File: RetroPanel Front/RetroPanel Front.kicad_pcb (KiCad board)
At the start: 2 copper layers, 100 x 22.9 mm, 11 parts, among them J1 Front Panel, M1 Mounting_Pin, M2 Mounting_Pin, M3 Mounting_Pin, M4 Mounting_Pin, SW1 TURBO, SW2 POWER, SW3 RESET, U1 3641AH

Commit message: Layout first draft
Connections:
- J1 pad 10: /7S_D1 -> /7S_F
- J1 pad 11: /7S_D2 -> /7S_E
- J1 pad 12: /7S_D3 -> /7S_D
- J1 pad 13: /7S_D4 -> /7S_DP
- J1 pad 14: SW_PWR1 -> /7S_C
- J1 pad 15: SW_PWR2 -> /7S_G
- J1 pad 16: LED_PWR1 -> /7S_D4
- J1 pad 17: LED_PWR2 -> /7S_D2
- J1 pad 18: SW_TURBO1 -> /7S_D3
- J1 pad 19: SW_TURBO2 -> /7S_B
- J1 pad 2: /7S_A -> SW_PWR1
- J1 pad 20: LED_TURBO1 -> SW_TURBO1
- J1 pad 21: LED_TURBO2 -> SW_TURBO2
- J1 pad 22: SW_RES1 -> LED_TURBO1
- J1 pad 23: SW_RES2 -> LED_TURBO2
- J1 pad 3: /7S_B -> SW_PWR2
- J1 pad 4: /7S_C -> LED_PWR1
- J1 pad 5: /7S_D -> LED_PWR2
- J1 pad 6: /7S_E -> SW_RESET1
- J1 pad 7: /7S_F -> SW_RESET2
- J1 pad 8: /7S_G -> /7S_D1
- J1 pad 9: /7S_DP -> /7S_A
- SW3 pad 2: SW_RES1 -> SW_RESET1
- SW3 pad 3: SW_RES2 -> SW_RESET2
- SW3 pad 5: SW_RES1 -> SW_RESET1
- SW3 pad 6: SW_RES2 -> SW_RESET2
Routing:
- net SW_TURBO1: track 0.00 -> 48.6 mm
- net LED_TURBO1: track 0.00 -> 38.7 mm
- net LED_PWR1: track 0.00 -> 32.0 mm
- net LED_TURBO2: track 0.00 -> 31.1 mm
- net LED_PWR2: track 0.00 -> 28.9 mm
- net /7S_D3: track 0.00 -> 23.7 mm
- net /7S_B: track 0.00 -> 23.7 mm
- net /7S_D2: track 0.00 -> 23.7 mm
- net SW_TURBO2: track 0.00 -> 23.4 mm
- net /7S_F: track 0.00 -> 21.3 mm
- net SW_PWR2: track 0.00 -> 21.1 mm
- net SW_RESET2: track 0.00 -> 21.1 mm
- net SW_PWR1: track 0.00 -> 19.0 mm
- net /7S_A: track 0.00 -> 18.6 mm
- net /7S_D1: track 0.00 -> 18.6 mm
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
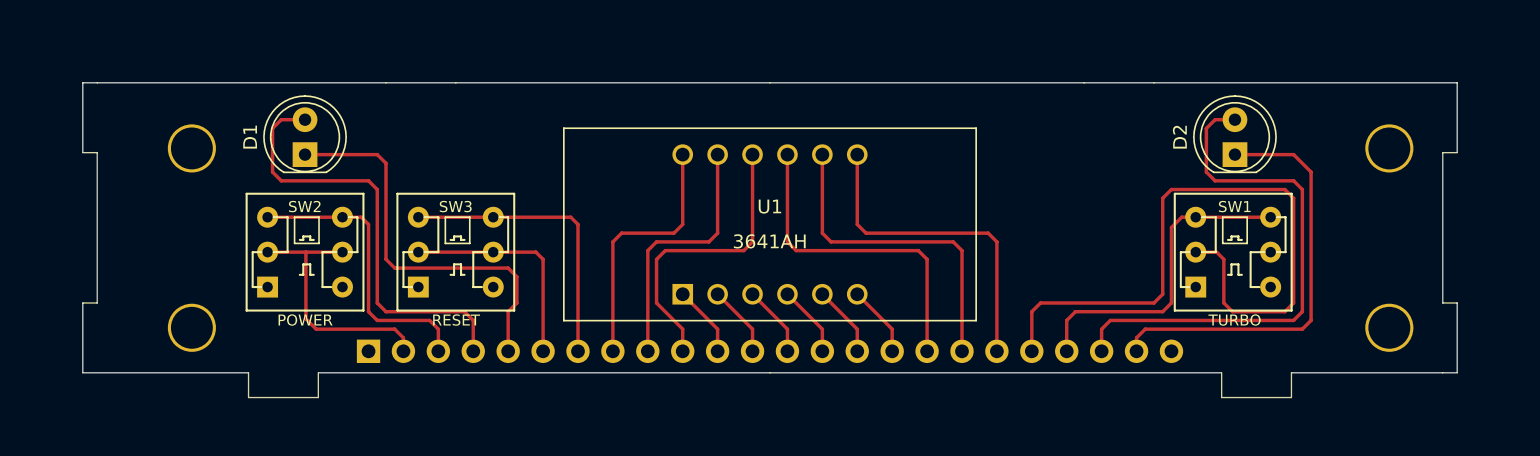
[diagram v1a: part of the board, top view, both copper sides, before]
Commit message: Add extra switch and tweak size
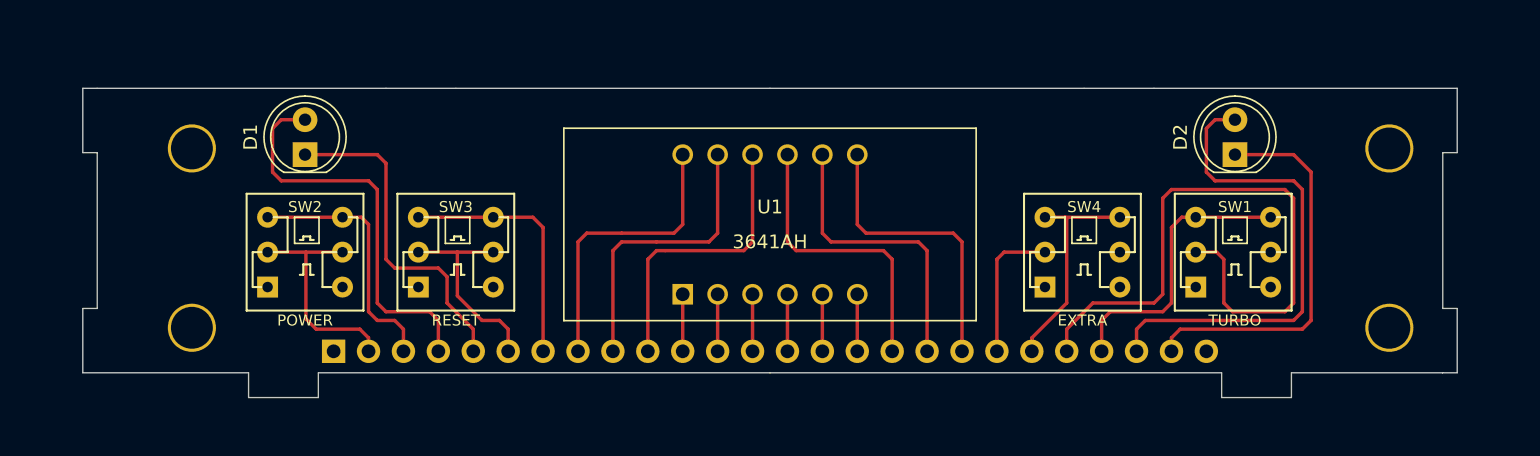
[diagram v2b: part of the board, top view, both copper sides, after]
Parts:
- added SW4: EXTRA, 6pin_switch:dpdt_switch_black, F.Cu at (163.8, 123.6)
- J1: footprint Connector_PinHeader_2.54mm:PinHeader_1x24_P2.54mm_Horizontal -> Connector_PinHeader_2.54mm:PinHeader_1x26_P2.54mm_Horizontal
- moved J1 2.54 mm to (109.3, 130.8)
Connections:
- J1 pad 20: SW_TURBO1 -> SW_EXTRA1
- J1 pad 21: SW_TURBO2 -> SW_EXTRA2
- J1 pad 22: LED_TURBO1 -> SW_TURBO1
- J1 pad 23: LED_TURBO2 -> SW_TURBO2
- J1 pad 24: GND -> LED_TURBO1
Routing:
- net SW_EXTRA2: track 0.00 -> 16.3 mm
- net SW_EXTRA1: track 0.00 -> 10.4 mm
- net LED_PWR2: track 28.9 -> 24.3 mm
- net SW_TURBO1: track 48.6 -> 45.3 mm
- net SW_RESET2: track 21.1 -> 18.4 mm
- net LED_TURBO2: track 31.1 -> 28.5 mm
- net /7S_D2: track 23.7 -> 21.2 mm
- net LED_TURBO1: track 38.7 -> 36.1 mm
- net SW_PWR1: track 19.0 -> 16.4 mm
- net LED_PWR1: track 32.0 -> 29.4 mm
- net /7S_D3: track 23.7 -> 21.2 mm
- net /7S_A: track 18.6 -> 21.2 mm
- net SW_PWR2: track 21.1 -> 18.6 mm
- net /7S_D1: track 18.6 -> 21.2 mm
- net SW_TURBO2: track 23.4 -> 20.9 mm
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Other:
- board size 100 x 22.9 mm -> 100 x 22.5 mm

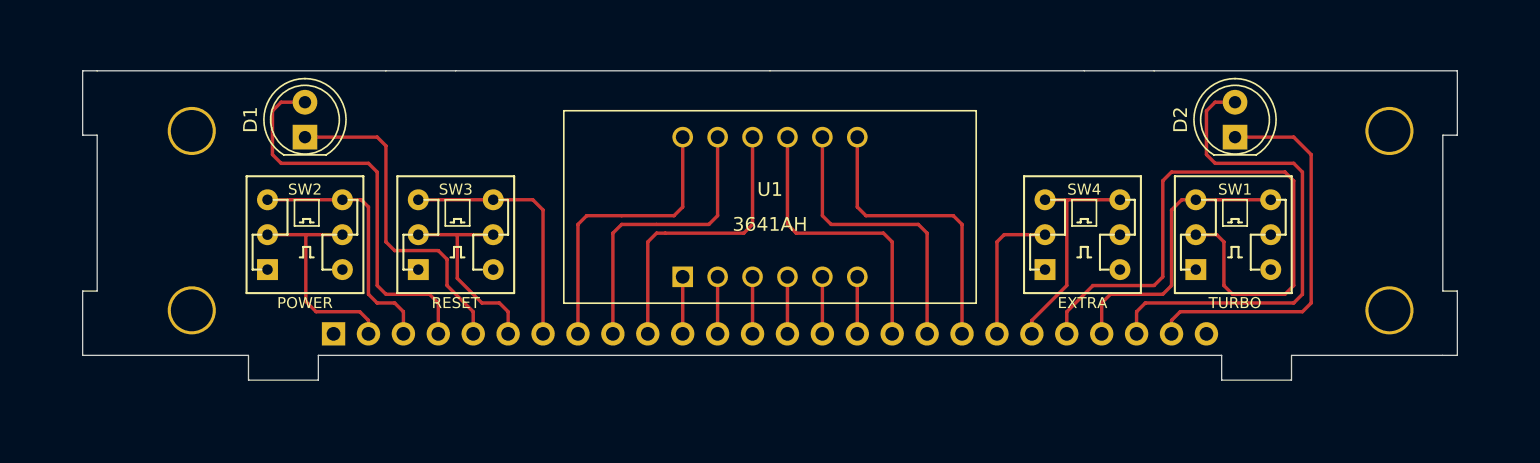
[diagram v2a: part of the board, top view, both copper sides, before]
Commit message: Add mounting pads
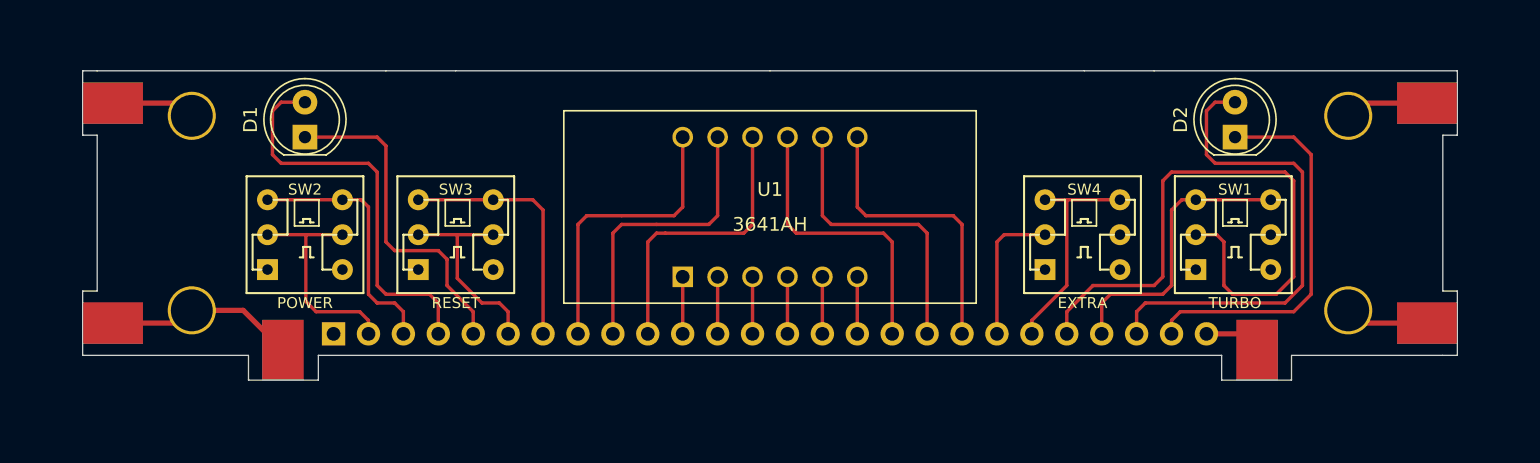
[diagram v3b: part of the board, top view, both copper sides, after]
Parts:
- added M10: Mounting_Pad, RetroPanel:Pad_pin, F.Cu at (188.9, 130.0)
- added M5: Mounting_Pad, RetroPanel:Pad_pin, F.Cu at (93.3, 114.0)
- added M6: Mounting_Pad, RetroPanel:Pad_pin, F.Cu at (176.5, 132.0)
- added M7: Mounting_Pad, RetroPanel:Pad_pin, F.Cu at (93.3, 130.0)
- added M8: Mounting_Pad, RetroPanel:Pad_pin, F.Cu at (105.7, 132.0)
- added M9: Mounting_Pad, RetroPanel:Pad_pin, F.Cu at (188.9, 114.0)
- moved M3 3.20 mm to (183.2, 114.9)
- moved M2 3.00 mm to (183.2, 129.1)
- moved M4 1.10 mm to (99.0, 114.9)
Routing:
- net GND: track 0.00 -> 36.5 mm

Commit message: Match grid
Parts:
- moved D2 33.8 mm to (184.6, 84.1)
- moved D1 33.8 mm to (116.9, 84.1)
- moved J1 33.8 mm to (119.0, 98.4)
- moved M1 33.8 mm to (108.7, 96.7)
- moved M10 33.8 mm to (198.6, 97.7)
- moved M2 33.8 mm to (192.8, 96.7)
- moved M3 33.8 mm to (192.8, 82.6)
- moved M4 33.8 mm to (108.7, 82.6)
- moved M5 33.8 mm to (102.9, 81.6)
- moved M6 33.8 mm to (186.2, 99.6)
- moved M7 33.8 mm to (102.9, 97.7)
- moved M8 33.8 mm to (115.3, 99.6)
- moved M9 33.8 mm to (198.6, 81.6)
- moved SW1 33.8 mm to (184.5, 91.2)
- moved SW2 33.8 mm to (116.9, 91.2)
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
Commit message: Rough layout of module
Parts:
- removed M6, M8: Mounting_Pad, RetroPanel:Pad_pin
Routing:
- net GND: track 36.5 -> 24.5 mm

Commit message: Faceplate FP1 and HDD LED
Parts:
- added D3: HDD, LED_THT:LED_D5.0mm, F.Cu at (173.5, 84.1)
- J1: footprint Connector_PinHeader_2.54mm:PinHeader_1x26_P2.54mm_Horizontal -> Connector_PinHeader_2.54mm:PinHeader_1x30_P2.54mm_Horizontal
- moved J1 5.08 mm to (113.9, 98.4)
- moved D2 0.13 mm to (184.5, 84.1)
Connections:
- J1 pad 10: /7S_F -> /7S_D1
- J1 pad 11: /7S_E -> /7S_A
- J1 pad 12: /7S_D -> /7S_F
- J1 pad 13: /7S_DP -> /7S_E
- J1 pad 14: /7S_C -> /7S_D
- J1 pad 15: /7S_G -> /7S_DP
- J1 pad 16: /7S_D4 -> /7S_C
- J1 pad 17: /7S_D2 -> /7S_G
- J1 pad 18: /7S_D3 -> /7S_D4
- J1 pad 19: /7S_B -> /7S_D2
- J1 pad 2: SW_PWR1 -> (no net)
- J1 pad 20: SW_EXTRA1 -> /7S_D3
- J1 pad 21: SW_EXTRA2 -> /7S_B
- J1 pad 22: SW_TURBO1 -> LED_HDD1
- J1 pad 23: SW_TURBO2 -> LED_HDD2
- J1 pad 24: LED_TURBO1 -> SW_EXTRA1
- J1 pad 25: LED_TURBO2 -> SW_EXTRA2
- J1 pad 26: GND -> SW_TURBO1
- J1 pad 3: SW_PWR2 -> (no net)
- J1 pad 4: LED_PWR1 -> SW_PWR1
- J1 pad 5: LED_PWR2 -> SW_PWR2
- J1 pad 6: SW_RESET1 -> LED_PWR1
- J1 pad 7: SW_RESET2 -> LED_PWR2
- J1 pad 8: /7S_D1 -> SW_RESET1
- J1 pad 9: /7S_A -> SW_RESET2
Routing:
- net LED_HDD1: track 0.00 -> 22.7 mm
- net LED_HDD2: track 0.00 -> 19.3 mm
- net LED_TURBO1: track 35.7 -> 30.5 mm
- net LED_TURBO2: track 28.2 -> 23.2 mm
- net SW_TURBO1: track 45.0 -> 40.3 mm
- net SW_TURBO2: track 20.9 -> 16.5 mm
- net SW_EXTRA1: track 10.4 -> 8.15 mm
- net SW_EXTRA2: track 16.3 -> 15.2 mm
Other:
- board text added: "3.5" RetroPanel Front (rev. A) github.com/tebl"
- board text removed: "RetroPanel Front (rev. A) github.com/tebl"

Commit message: Bumped version
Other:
- board text added: "3.5" RetroPanel Front (rev. B) github.com/tebl"
- board text removed: "3.5" RetroPanel Front (rev. A) github.com/tebl"
